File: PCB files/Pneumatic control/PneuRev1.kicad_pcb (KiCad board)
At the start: 2 copper layers, 230.9 x 135.6 mm, 50 parts, among them J1 SIG_IN, J2 BATT_IN, J3 PNEU, U1 uA7824, U2 OP279, U3 OP279, U4 OP279, U5 OP279, U6 OP279, U7 OP279, U8 OP07

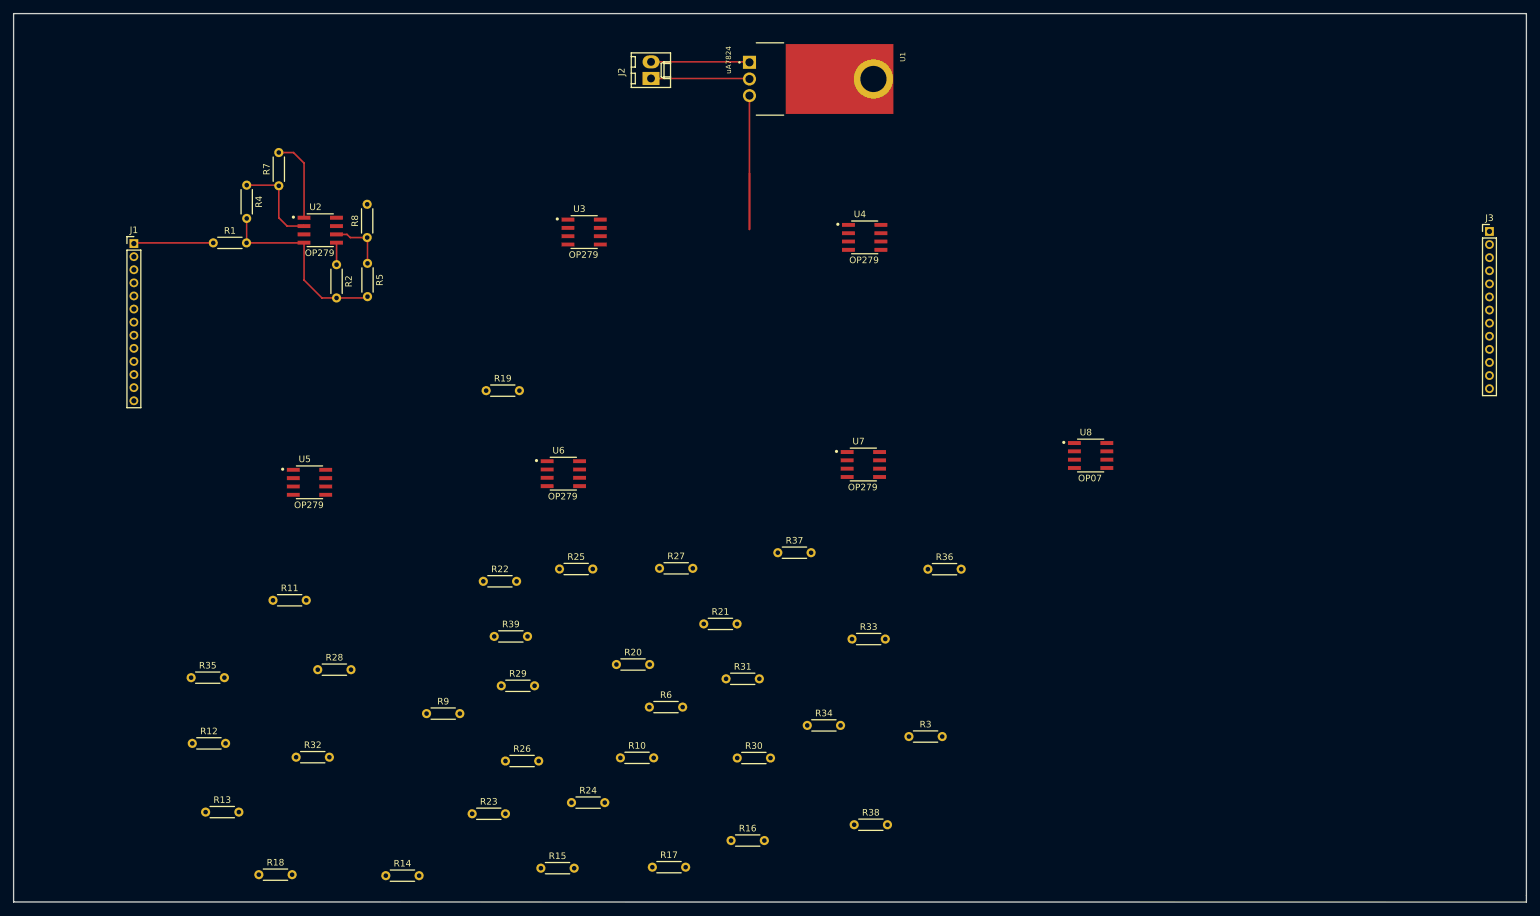
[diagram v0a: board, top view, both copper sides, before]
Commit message: 1/31/2019
-Added battery power indicator LED
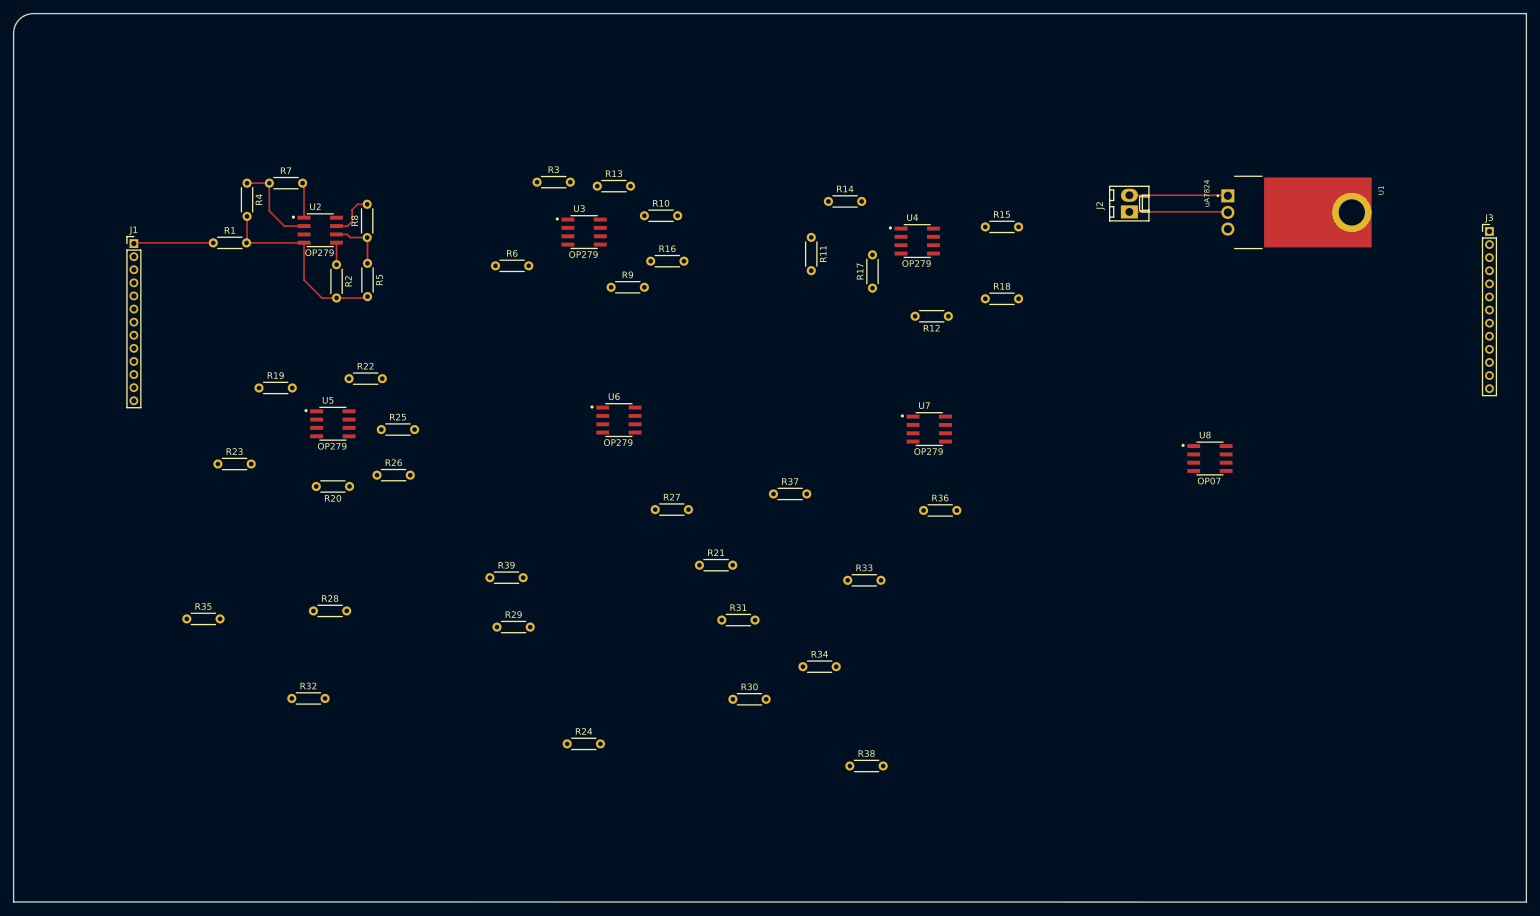
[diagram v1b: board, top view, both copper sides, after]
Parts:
- moved R18 141.5 mm to (183.4, 71.6)
- moved R12 132.6 mm to (177.7, 74.2), turned to 180 degrees
- moved R14 123.1 mm to (159.4, 56.7)
- moved R15 119.1 mm to (183.4, 60.6)
- moved R13 112.7 mm to (124.2, 54.4)
- moved R3 101.9 mm to (115.0, 53.7)
- moved R11 99.1 mm to (156.8, 62.2), turned to 270 degrees
- moved R17 94.6 mm to (166.2, 69.9), turned to 90 degrees
- moved R16 89.3 mm to (132.3, 65.8)
- moved R10 82.8 mm to (131.3, 58.9)
- moved J2 75.8 mm to (205.4, 58.3)
- moved U1 75.8 mm to (220.4, 55.8)
- moved R6 71.3 mm to (108.6, 66.5)
- moved R9 70.9 mm to (126.3, 69.8)
- moved R23 66.0 mm to (66.2, 96.8)
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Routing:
- net Net-(U1-Pad3): track 29.0 -> 0.00 mm
- net /PNU1: track 12.9 -> 5.37 mm
- net /PNU2: track 0.00 -> 7.11 mm
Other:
- outline, holes or cut-outs redrawn

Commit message: 1/31/2019
-Gave board edge round corners
-Routed traces for PWR input part of the board
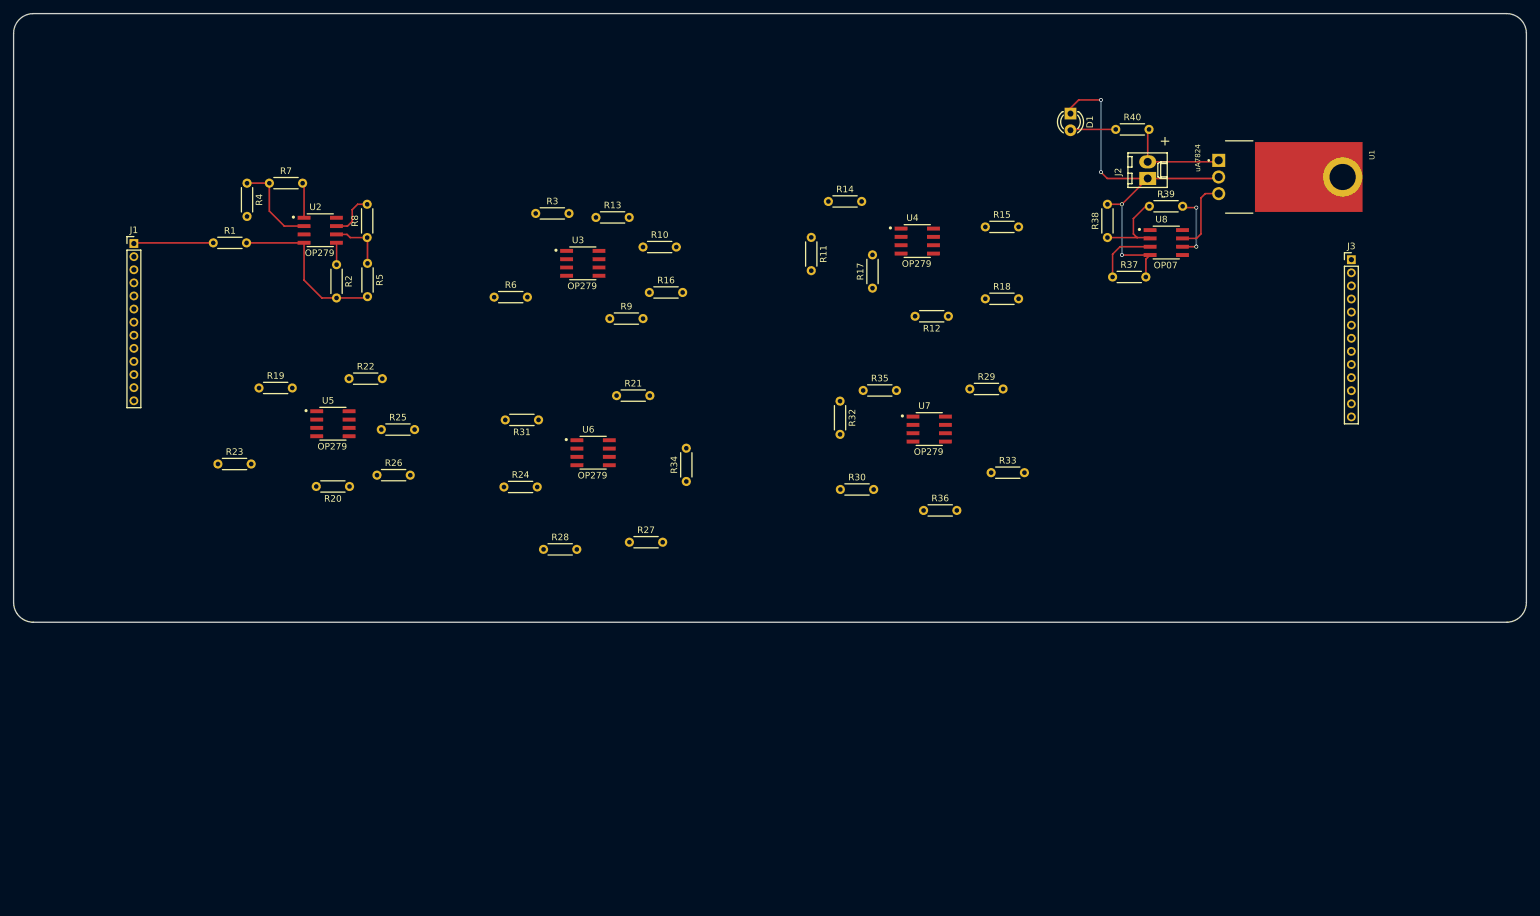
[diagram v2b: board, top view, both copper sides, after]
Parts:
- added D1: LED, LEDs:LED_D3.0mm, F.Cu at (196.4, 43.3)
- added R40: 3k5, Resistors_THT:R_Axial_DIN0204_L3.6mm_D1.6mm_P5.08mm_Horizontal, F.Cu at (203.3, 45.7)
- moved R39 115.5 mm to (208.4, 57.4)
- moved R35 109.0 mm to (164.7, 85.5)
- moved R32 95.2 mm to (161.2, 87.2), turned to 270 degrees
- moved R38 89.7 mm to (202.0, 62.2), turned to 90 degrees
- moved R29 80.8 mm to (181.0, 85.3)
- moved R37 61.5 mm to (202.8, 68.2)
- moved R31 41.4 mm to (115.2, 90.0), turned to 180 degrees
- moved R24 40.4 mm to (109.9, 100.3)
- moved R28 36.4 mm to (116.0, 109.8)
- moved R30 36.0 mm to (161.3, 100.7)
- moved U8 33.6 mm to (211.0, 63.0)
- moved R34 33.4 mm to (137.7, 99.4), turned to 90 degrees
- moved R21 28.8 mm to (127.1, 86.3)
- moved R33 27.4 mm to (184.3, 98.1)
- moved J3 21.5 mm to (239.3, 65.6)
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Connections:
- J2 pad 1: Net-(J2-Pad1) -> GND
- U1 pad 2: Net-(J2-Pad1) -> GND
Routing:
- net GND: track 29.5 -> 84.6 mm, vias 0 -> 4
- net Net-(J2-Pad1): track 15.1 -> 0.00 mm
- net Net-(R38-Pad1): track 0.00 -> 12.9 mm
- net Net-(U1-Pad3): track 0.00 -> 11.6 mm
- net /PNU13: track 0.00 -> 10.2 mm, vias 0 -> 2
- net /IN13: track 0.00 -> 9.67 mm
- net Net-(D1-Pad2): track 0.00 -> 6.96 mm
- net Net-(J2-Pad2): track 15.1 -> 16.1 mm
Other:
- board size 230.9 x 135.6 mm -> 230.9 x 92.9 mm
- board text added: "+"
- board text added: "-"

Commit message: 1/31/2019
-Continued routing board
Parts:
- moved J2 122.4 mm to (89.3, 82.6)
- moved R40 112.8 mm to (94.3, 74.6), turned to 180 degrees
- moved D1 98.7 mm to (102.9, 74.6), turned to 180 degrees
- moved R38 83.8 mm to (118.5, 69.8)
- moved R39 83.8 mm to (124.9, 65.1)
- moved U8 83.8 mm to (127.5, 70.6)
- moved R37 83.8 mm to (119.3, 75.9)
- moved R23 58.9 mm to (120.6, 119.3), turned to 270 degrees
- moved J3 56.5 mm to (212.1, 115.1), turned to 180 degrees
- moved R31 53.1 mm to (157.1, 122.7), turned to 270 degrees
- moved U1 51.0 mm to (171.2, 68.1)
- moved R13 46.5 mm to (154.3, 94.4), turned to 270 degrees
- moved R7 46.0 mm to (110.6, 81.8)
- moved J1 41.1 mm to (83.4, 91.1)
- moved R1 41.1 mm to (95.6, 91.0)
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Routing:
- net /IN3: track 0.00 -> 70.8 mm, vias 0 -> 2
- net /IN9: track 0.00 -> 56.2 mm, vias 0 -> 2
- net GND: track 84.6 -> 36.1 mm, vias 4 -> 2
- net Net-(U1-Pad3): track 11.6 -> 46.9 mm, vias 0 -> 2
- net /PNU3: track 0.00 -> 18.2 mm
- net /IN7: track 0.00 -> 13.7 mm
- net Net-(R23-Pad1): track 0.00 -> 12.8 mm
- net Net-(R22-Pad1): track 0.00 -> 12.6 mm
- net Net-(R13-Pad1): track 0.00 -> 11.3 mm
- net Net-(J2-Pad2): track 16.1 -> 5.43 mm
- net /PNU8: track 0.00 -> 8.50 mm
- net /IN8: track 0.00 -> 5.09 mm
- net /IN12: track 0.00 -> 4.00 mm
- net Net-(R4-Pad1): track 14.0 -> 10.0 mm
- net /PNU1: track 5.37 -> 9.34 mm
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- added copper zone on F.Cu, net GND
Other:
- board size 230.9 x 92.9 mm -> 145.7 x 92.9 mm
- board text removed: "+"
- board text removed: "-"

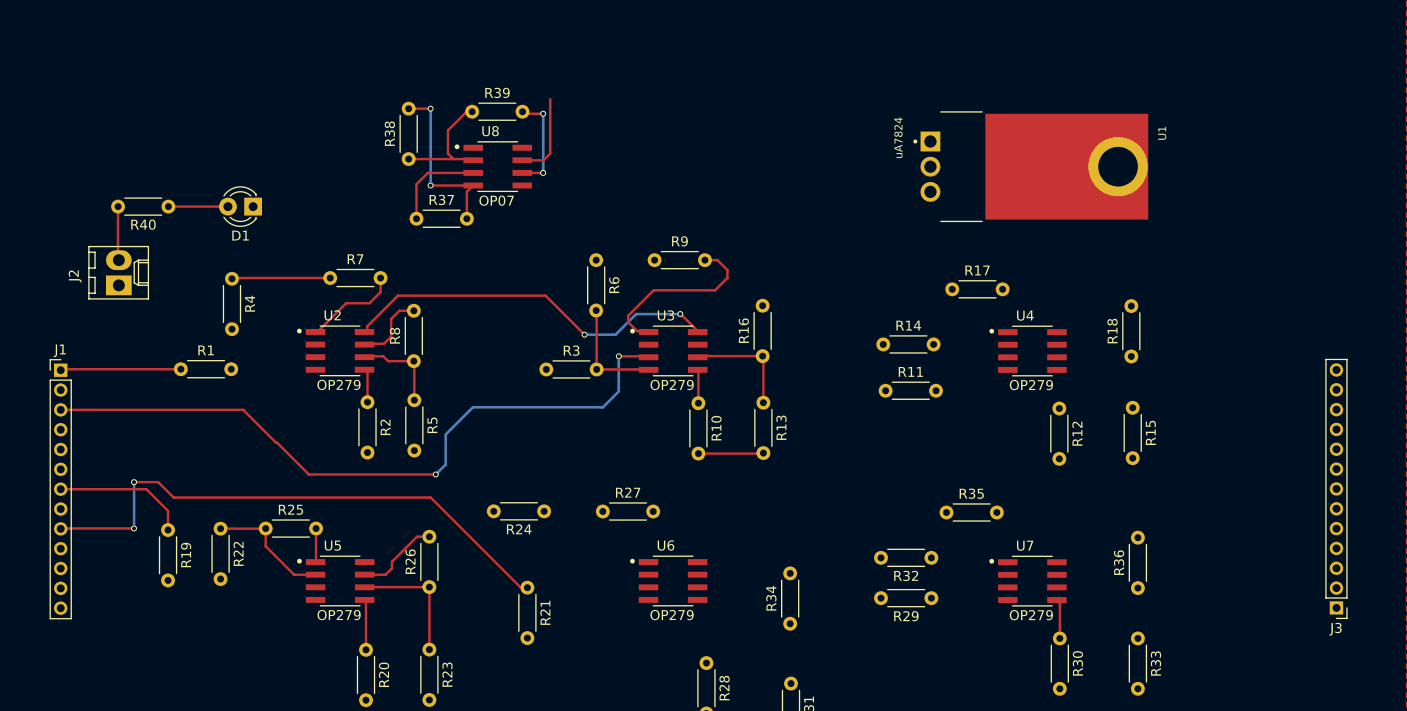
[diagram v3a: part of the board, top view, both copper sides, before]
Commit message: 2/4/2019
-Fixed schematic opamp numbering issue
-Relabelled LED limit resistor to 3k
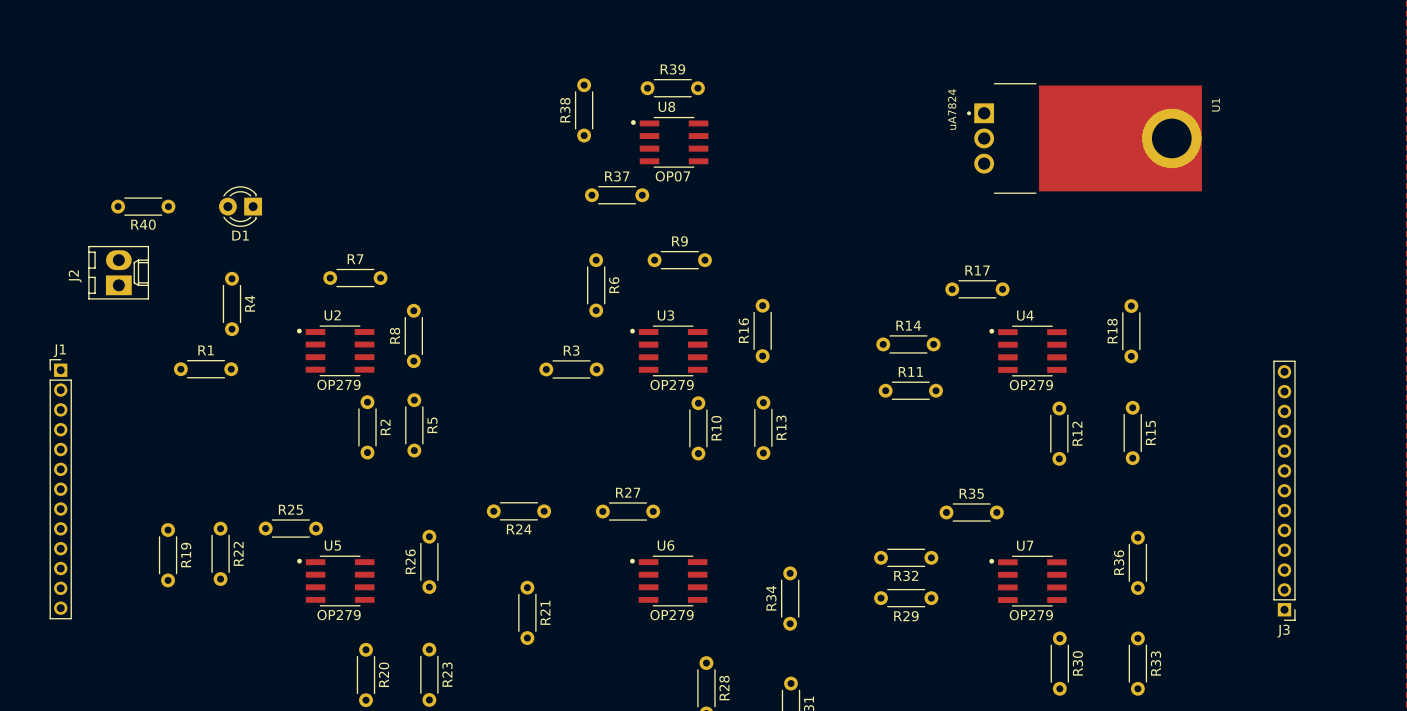
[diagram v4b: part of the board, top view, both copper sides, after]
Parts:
- R40: value 3k5 -> 3k
- moved U8 18.0 mm to (145.3, 68.1)
- moved R37 17.9 mm to (137.0, 73.5)
- moved R38 17.9 mm to (136.2, 67.5)
- moved R39 17.9 mm to (142.6, 62.7)
- moved U1 6.12 mm to (176.6, 65.2)
- moved J3 5.25 mm to (206.9, 115.3)
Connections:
- U2 pad 1: /PNU1 -> Net-(J1-Pad1)
- U2 pad 2: Net-(R4-Pad1) -> GND
- U2 pad 3: Net-(J1-Pad1) -> /IN2
- U2 pad 4: GND -> Net-(R5-Pad1)
- U2 pad 5: /IN2 -> /PNU2
- U2 pad 6: Net-(R5-Pad1) -> Net-(U1-Pad3)
- U2 pad 7: /PNU2 -> /PNU1
- U2 pad 8: Net-(U1-Pad3) -> Net-(R4-Pad1)
- U3 pad 1: /PNU3 -> /IN3
- U3 pad 2: Net-(R6-Pad1) -> GND
- U3 pad 3: /IN3 -> /IN4
- U3 pad 4: GND -> Net-(R13-Pad1)
- U3 pad 5: /IN4 -> /PNU4
- U3 pad 6: Net-(R13-Pad1) -> Net-(U1-Pad3)
- U3 pad 7: /PNU4 -> /PNU3
- U3 pad 8: Net-(U1-Pad3) -> Net-(R6-Pad1)
- U4 pad 1: /PNU5 -> /IN5
- U4 pad 2: Net-(R14-Pad1) -> GND
- U4 pad 3: /IN5 -> /IN6
- U4 pad 4: GND -> Net-(R15-Pad1)
- U4 pad 5: /IN6 -> /PNU6
- U4 pad 6: Net-(R15-Pad1) -> Net-(U2-Pad6)
- U4 pad 7: /PNU6 -> /PNU5
- U4 pad 8: Net-(U2-Pad8) -> Net-(R14-Pad1)
- U5 pad 1: /PNU7 -> /IN7
- U5 pad 2: Net-(R22-Pad1) -> GND
- U5 pad 3: /IN7 -> /IN8
- U5 pad 4: GND -> Net-(R23-Pad1)
- U5 pad 5: /IN8 -> /PNU8
- U5 pad 6: Net-(R23-Pad1) -> Net-(U1-Pad3)
- U5 pad 7: /PNU8 -> /PNU7
- U5 pad 8: Net-(U1-Pad3) -> Net-(R22-Pad1)
- U6 pad 1: /PNU9 -> /IN9
- U6 pad 2: Net-(R24-Pad1) -> GND
- U6 pad 3: /IN9 -> /IN10
- U6 pad 4: GND -> Net-(R31-Pad1)
- U6 pad 5: /IN10 -> /PNU10
- U6 pad 6: Net-(R31-Pad1) -> Net-(U1-Pad3)
- U6 pad 7: /PNU10 -> /PNU9
- U6 pad 8: Net-(U1-Pad3) -> Net-(R24-Pad1)
- U7 pad 1: /PNU11 -> /IN11
- U7 pad 2: Net-(R32-Pad1) -> GND
- U7 pad 3: /IN11 -> /IN12
- U7 pad 4: GND -> Net-(R33-Pad1)
- U7 pad 5: /IN12 -> /PNU12
- U7 pad 6: Net-(R33-Pad1) -> Net-(U2-Pad6)
- U7 pad 7: /PNU12 -> /PNU11
- U7 pad 8: Net-(U2-Pad8) -> Net-(R32-Pad1)
- U8 pad 1: Net-(U8-Pad1) -> /IN13
- U8 pad 2: Net-(R38-Pad1) -> GND
- U8 pad 3: /IN13 -> Net-(U8-Pad3)
- U8 pad 4: GND -> Net-(U8-Pad4)
- U8 pad 6: /PNU13 -> Net-(U1-Pad3)
- U8 pad 7: Net-(U1-Pad3) -> /PNU13
- U8 pad 8: Net-(U8-Pad8) -> Net-(R38-Pad1)
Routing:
- net /IN3: track 70.8 -> 0.00 mm, vias 2 -> 0
- net /IN9: track 56.2 -> 0.00 mm, vias 2 -> 0
- net Net-(U1-Pad3): track 46.9 -> 0.00 mm, vias 2 -> 0
- net GND: track 36.1 -> 0.00 mm, vias 2 -> 0
- net /PNU3: track 18.2 -> 0.00 mm
- net /IN7: track 13.7 -> 0.00 mm
- net Net-(R38-Pad1): track 12.9 -> 0.00 mm
- net Net-(R23-Pad1): track 12.8 -> 0.00 mm
- net Net-(R22-Pad1): track 12.6 -> 0.00 mm
- net Net-(J1-Pad1): track 12.2 -> 0.00 mm
- net Net-(R13-Pad1): track 11.3 -> 0.00 mm
- net /PNU13: track 10.2 -> 0.00 mm, vias 2 -> 0
- net Net-(R4-Pad1): track 10.0 -> 0.00 mm
- net /IN13: track 9.67 -> 0.00 mm
- net /PNU1: track 9.34 -> 0.00 mm
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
